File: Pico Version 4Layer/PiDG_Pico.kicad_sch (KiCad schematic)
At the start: 77 parts, among them J1 Conn_02x05_Odd_Even, J10 Trig, J11 Laser Enable, J12 Pixel Reset, J14 Pico Socket A, J15 Pico Socket B, J16 Laser En/PWM Trig/GND, J17 USB-C PD in, J2 Conn_02x05_Odd_Even, J3 Conn_02x05_Odd_Even, J4 Conn_02x05_Odd_Even, J5 Conn_02x05_Odd_Even, J6 Conn_02x05_Odd_Even, J7 Laser 1, J8 Laser 2, U1 74LVC1G04, U10 74AHCT1G08, U11 Raspberry Pi Pico 2 W, U12 74LVC1G17, U13 UCC27524, U14 CH224K, U15 AP63205WU, U16 LM66100, U17 LT3065EDD, U18 TPS3700DDC, U2 SN74LVC04AD, U3 74LVC1G00, U4 SN74LVC04AD, U5 74LVC1G04, U6 SN74LVC04AD, U7 74AHCT1G08, U8 74AHCT1G08, U9 NCP718xSN180

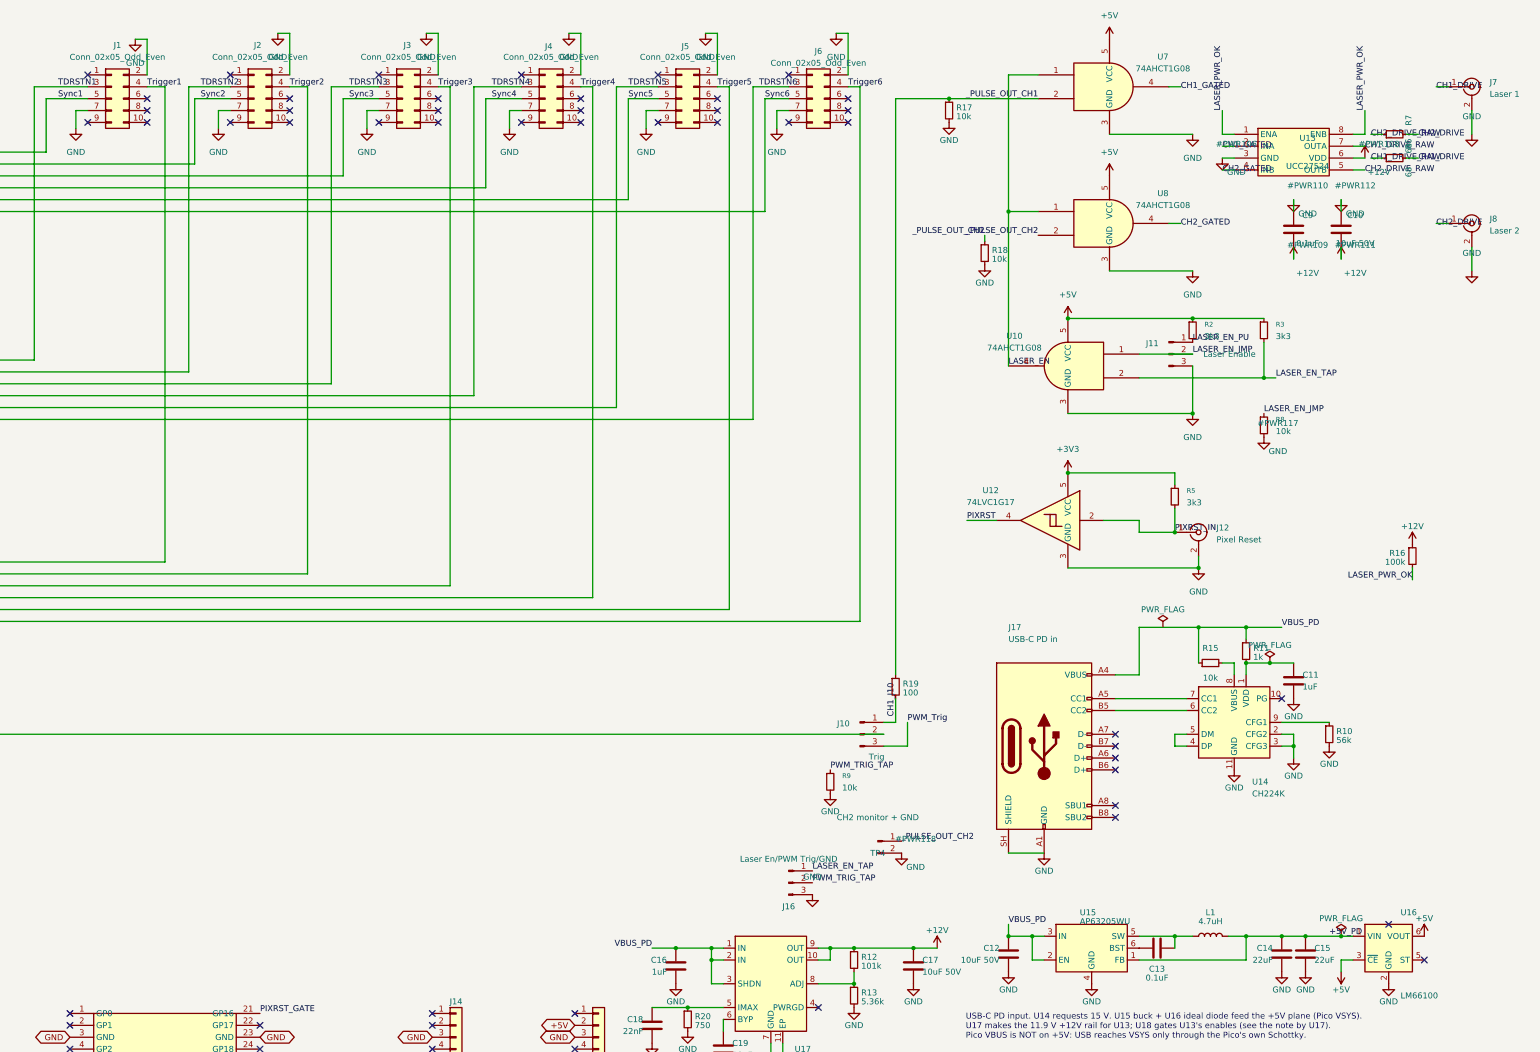
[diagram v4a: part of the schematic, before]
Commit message: Laser outputs: jumper-selectable 50 ohm / Hi-Z mode per channel
Each laser output gets a 1x3 mode jumper (J18 = Laser 1 / J7, J19 = Laser 2 /
J8), a 47 ohm series resistor (R25/R26) and an 82 ohm shunt to GND (R27/R28),
all 2 W 2512.
- 1-2, 50 ohm mode: the 47 ohm is shorted, so the output is unchanged:
  4.61-5.08 V into the 50 ohm LDP-V input, ~12 V open circuit.
- 2-3, Hi-Z mode: 47 ohm series + 82 ohm shunt give 4.62-5.06 V open circuit
  from a 47.8-49.6 ohm source, i.e. back-terminated, so a long cable into an
  unterminated input has no overshoot (<= 1.02x, 5.14 V max). Into 50 ohm it
  gives 2.3-2.6 V (an LDP-V will not fire).

Board: the blocks sit in the free strip between R6/R7 and the BNCs, with the
series resistor inline on each BNC centre-pin row, orthogonal/45-degree
routing, and channel 2 mirroring channel 1. New silk LASER n OUT / 50Ω / HiZ;
the J10 legend moved below J10. The pre-existing 27-degree CH2_DRIVE_RAW
segment into R7 is now an orthogonal/45-degree jog. Schematic: J7/J8 moved
inside the drawing frame into a new output-mode block with a note.

Checks: ERC 0; DRC 0 violations, 0 unconnected; schematic parity: no real net
conflicts (199 benign warnings, up from 187 for the new pads). Netlist diff
shows only the intended nets. Fab: BOM 43 lines / 82 parts (R25/R26 C5843114,
R27/R28 C7468298, J18/J19 on the C49257 header line); CPLs, gerbers, drill
files and zip regenerated. Docs: README, Hardware.md, JLC_ORDER.md, BOM notes.
Also corrects the stuck-high-into-a-short dissipation of R6/R7 in the docs
(1.6-2.05 W, not 1.9 W; <= 1.4 W at the firmware's maximum duty).

Reviewed by a five-lens adversarial workflow; its confirmed findings are fixed.

Co-Authored-By: Claude Opus 5.5 (1M context) <noreply@anthropic.com>
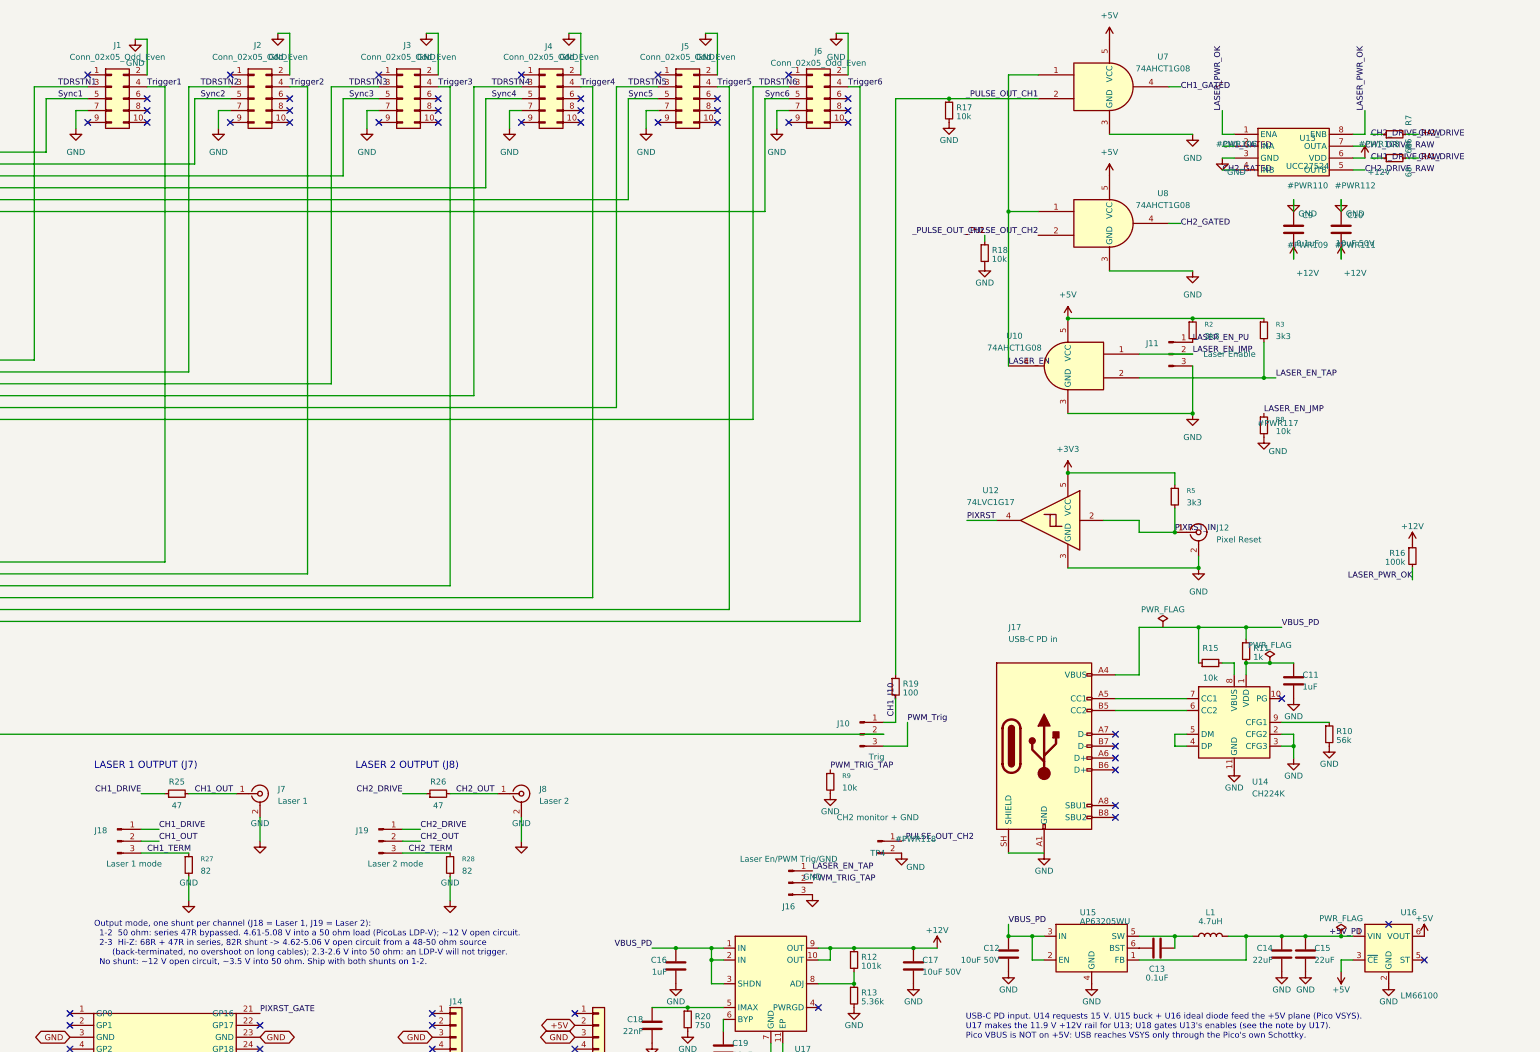
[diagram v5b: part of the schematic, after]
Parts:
- added J18: Laser 1 mode, Connector_PinHeader_2.54mm:PinHeader_1x03_P2.54mm_Vertical, symbol Connector:Conn_01x03_Pin
- added J19: Laser 2 mode, Connector_PinHeader_2.54mm:PinHeader_1x03_P2.54mm_Vertical, symbol Connector:Conn_01x03_Pin
- added R25, R26: 47, Resistor_SMD:R_2512_6332Metric_Pad1.40x3.35mm_HandSolder, symbol Device:R_Small
- added R27, R28: 82, Resistor_SMD:R_2512_6332Metric_Pad1.40x3.35mm_HandSolder, symbol Device:R_Small
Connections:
- net CH1_DRIVE: now also J18.1 (Pin_1), R25.1; no longer J7.1 (In)
- net CH2_DRIVE: now also J19.1 (Pin_1), R26.1; no longer J8.1 (In)
- net GND: now also R27.2, R28.2
- new net CH1_OUT: J18.2 (Pin_2), J7.1 (In), R25.2
- new net CH1_TERM: J18.3 (Pin_3), R27.1
- new net CH2_OUT: J19.2 (Pin_2), J8.1 (In), R26.2
- new net CH2_TERM: J19.3 (Pin_3), R28.1
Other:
- note added: "LASER 1 OUTPUT (J7)"
- note added: "LASER 2 OUTPUT (J8)"
- note added: "Output mode, one shunt per channel (J18 = Laser 1, J19 = Laser 2): 1-2 50 ohm: series 47R bypassed. 4.61-5.08 V into a 50 ohm load (PicoLas LDP-V); ~12 V open circuit. 2-3 Hi-Z: 68R + 47R in series, 82R shunt -> 4.62-5.06 V open circuit from a 48-50 ohm source (back-terminated, no overshoot on long cables); 2.3-2.6 V into 50 ohm: an LDP-V will not trigger. No shunt: ~12 V open circuit, ~3.5 V int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"
- moved on the sheet: J7, J8
